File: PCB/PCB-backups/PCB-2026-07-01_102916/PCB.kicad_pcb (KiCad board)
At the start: 2 copper layers, 31 x 42.5 mm, 5 parts, among them U1 XIAO-ESP32-S3-SMD, U3 adafruit-MAX98357

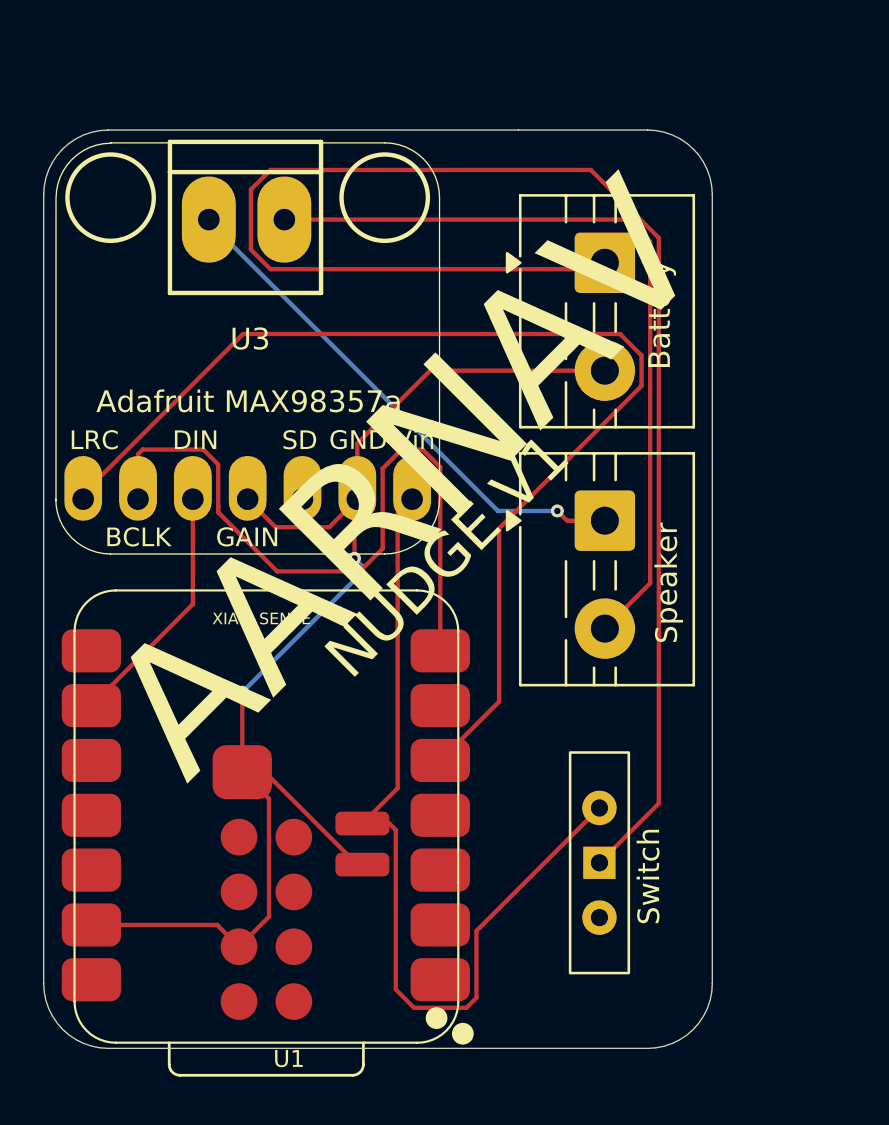
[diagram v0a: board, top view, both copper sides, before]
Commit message: Changed Silkscreen, PCB Up To Date
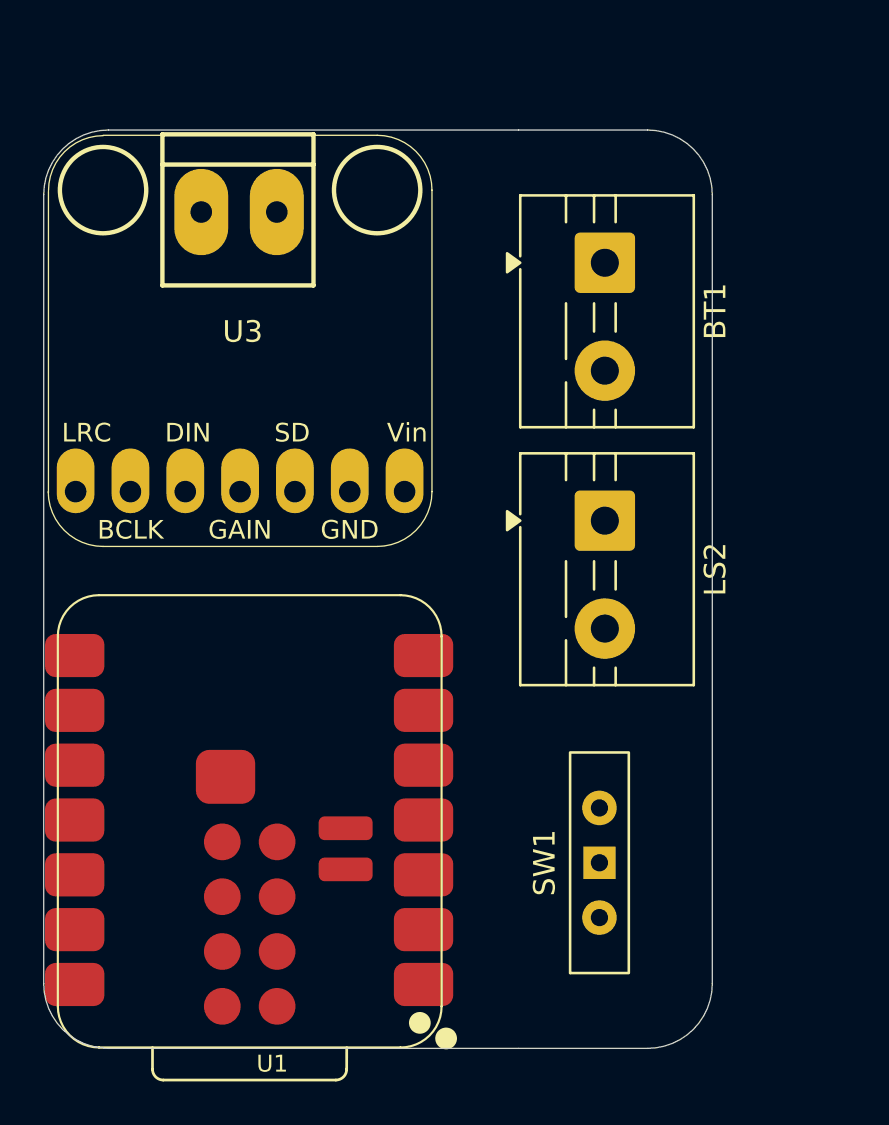
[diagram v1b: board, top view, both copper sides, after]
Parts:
- moved U1 0.81 mm to (194.3, 86.9)
- moved U3 0.49 mm to (185.1, 75.3)
- renumbered Switch to SW1
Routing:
- net Net-(BT1-+): track 70.4 -> 0.00 mm
- net GND: track 60.6 -> 0.00 mm, vias 2 -> 0
- net D4: track 52.2 -> 0.00 mm
- net VBAT: track 40.5 -> 0.00 mm
- net Net-(U3-OUTN): track 36.2 -> 0.00 mm
- net D6: track 33.3 -> 0.00 mm
- net Net-(U3-OUTP): track 24.2 -> 0.00 mm, vias 1 -> 0
- net D8: track 11.5 -> 0.00 mm
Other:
- board text removed: "AARNAV"
- board text removed: "Adafruit MAX98357a"
- board text removed: "Battery"
- board text removed: "NUDGE V1"
- board text removed: "Speaker"
- board text removed: "XIAO_SENSE"
